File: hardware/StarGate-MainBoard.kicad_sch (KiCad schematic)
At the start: 168 parts, among them IC1 TB6612FNG, IC3 TB6612FNG, IC7 SGTL5000, J1 PJ-037A, J10 Conn_01x02_Pin, J11 Conn_01x03_Male, J12 Conn_01x02_Pin, J13 Conn_01x02_Pin, J14 Conn_01x02_Pin, J15 Conn_01x02_Pin, J16 Conn_01x02_Pin, J17 Conn_01x02_Pin, J18 Conn_01x02_Pin, J19 Conn_01x02_Pin, J2 Conn_01x03_Socket, J20 Conn_01x02_Pin, J21 Conn_01x02_Pin, J22 Conn_01x02_Pin, J23 Conn_01x02_Pin, J24 Conn_01x03_Socket, J26 Micro_SD_Card_Det, J27 Conn_01x03_Male, J28 Conn_01x02_Pin, J29 Conn_01x02_Pin, J3 Conn_01x02_Pin, J30 Conn_01x02_Pin, J31 Conn_01x02_Pin, J32 Conn_01x03_Male, J33 Conn_01x02_Pin, J34 USB_C_Receptacle, J4 Conn_01x04_Pin, J5 Conn_01x02_Pin, J6 Conn_01x02_Pin, J7 Conn_01x02_Pin, J8 Conn_01x02_Pin, J9 Conn_01x02_Pin, Q1 FDN340P, Q12 PMOS, Q2 FDN337N, Q3 N0400P-ZK-E1-AY, SW1 SW_Push_Dual, SW2 SW_Push_Dual, U1 SN74LVC1T45DBV, U10 AZ1084-1.8, U11 USBLC6-4SC6, U12 STMPS2151STR, U2 PCA9685, U32 FM6124, U6 ESP32-S3-WROOM-1-N16R2, U7 MC33063ADR, U8 TPA6017A2, U9 RT6219, X1 SG-210SDF (11.2896MHz)

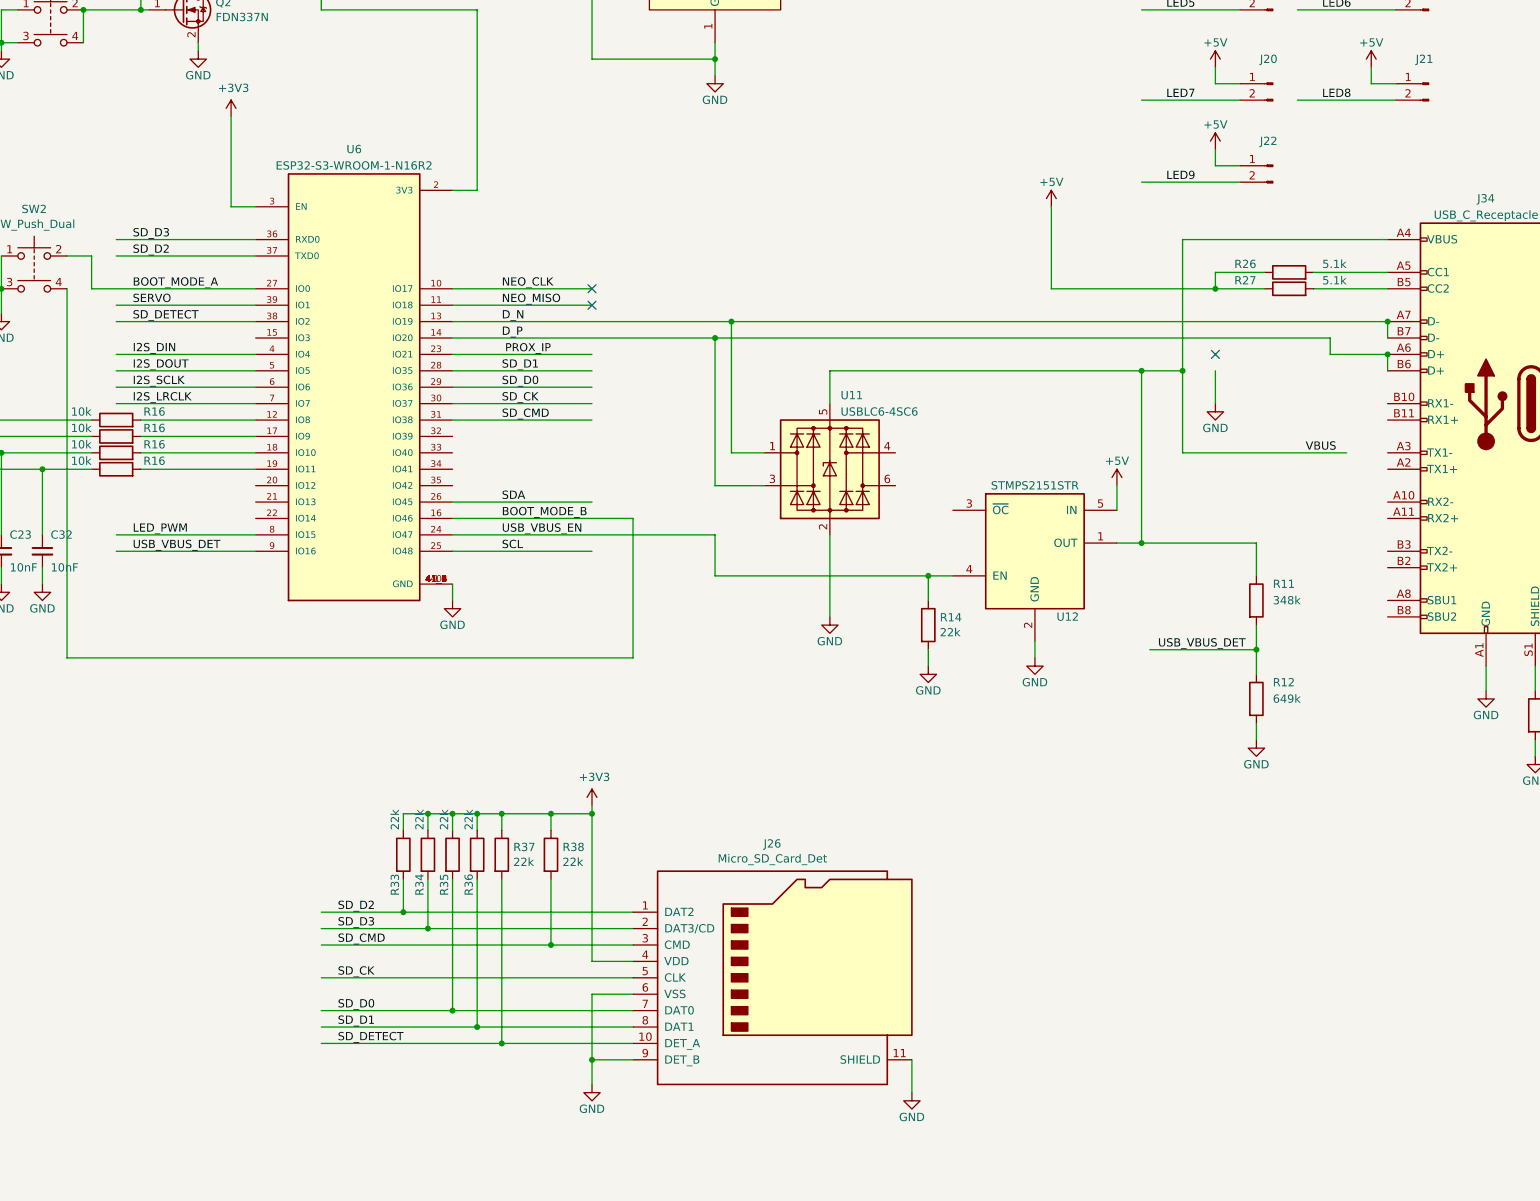
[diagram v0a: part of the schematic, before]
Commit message: Added JTAG Port
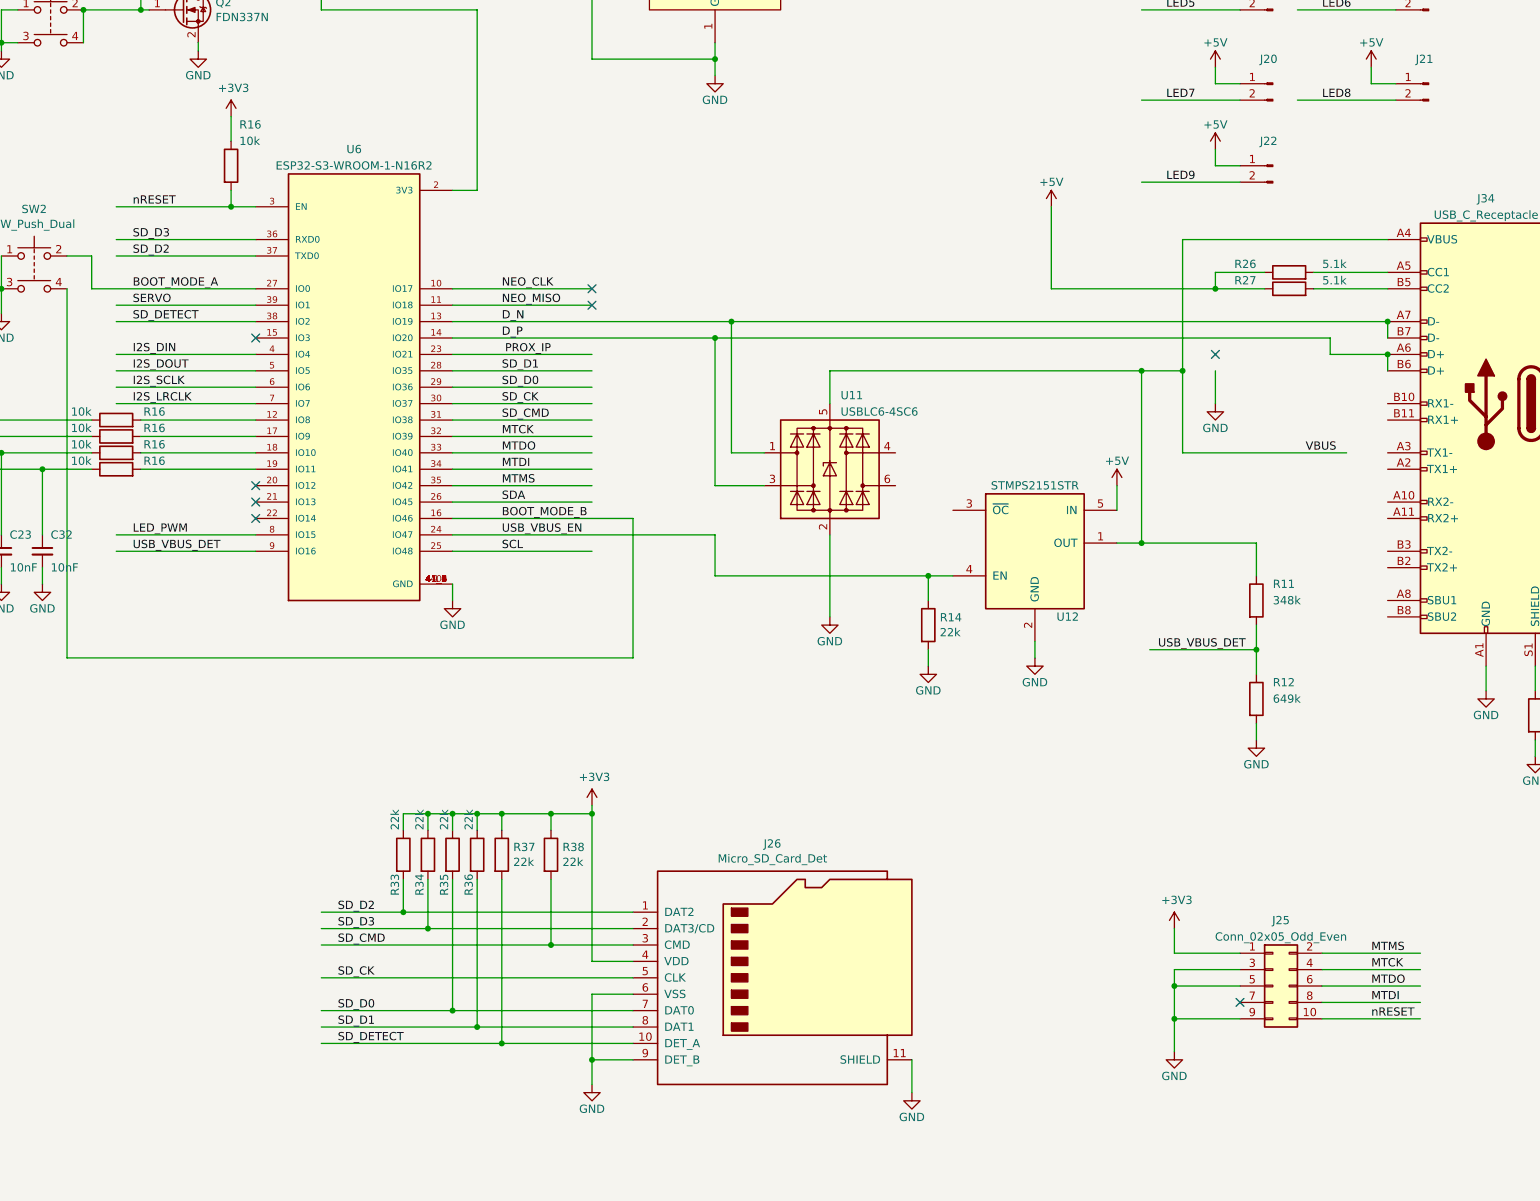
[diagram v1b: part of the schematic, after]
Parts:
- added J25: Conn_02x05_Odd_Even, Connector_PinHeader_2.54mm:PinHeader_2x05_P2.54mm_Vertical, symbol Connector_Generic:Conn_02x05_Odd_Even
- added R16: 10k, Resistor_SMD:R_0603_1608Metric, symbol Device:R
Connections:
- net +3V3: now also J25.1 (Pin_1), R16.1; no longer U6.3 (EN)
- net GND: now also J25.3 (Pin_3), J25.5 (Pin_5), J25.9 (Pin_9)
- net MTCK: now reaches U6.32 (IO39)
- net MTCK: now also J25.4 (Pin_4)
- net MTDO: now reaches U6.33 (IO40)
- net MTDO: now also J25.6 (Pin_6)
- net MTDI: now reaches U6.34 (IO41)
- net MTDI: now also J25.8 (Pin_8)
- net MTMS: now reaches U6.35 (IO42)
- net MTMS: now also J25.2 (Pin_2)
- new net nRESET: J25.10 (Pin_10), R16.2, U6.3 (EN)
- no-connect marks 38 -> 43

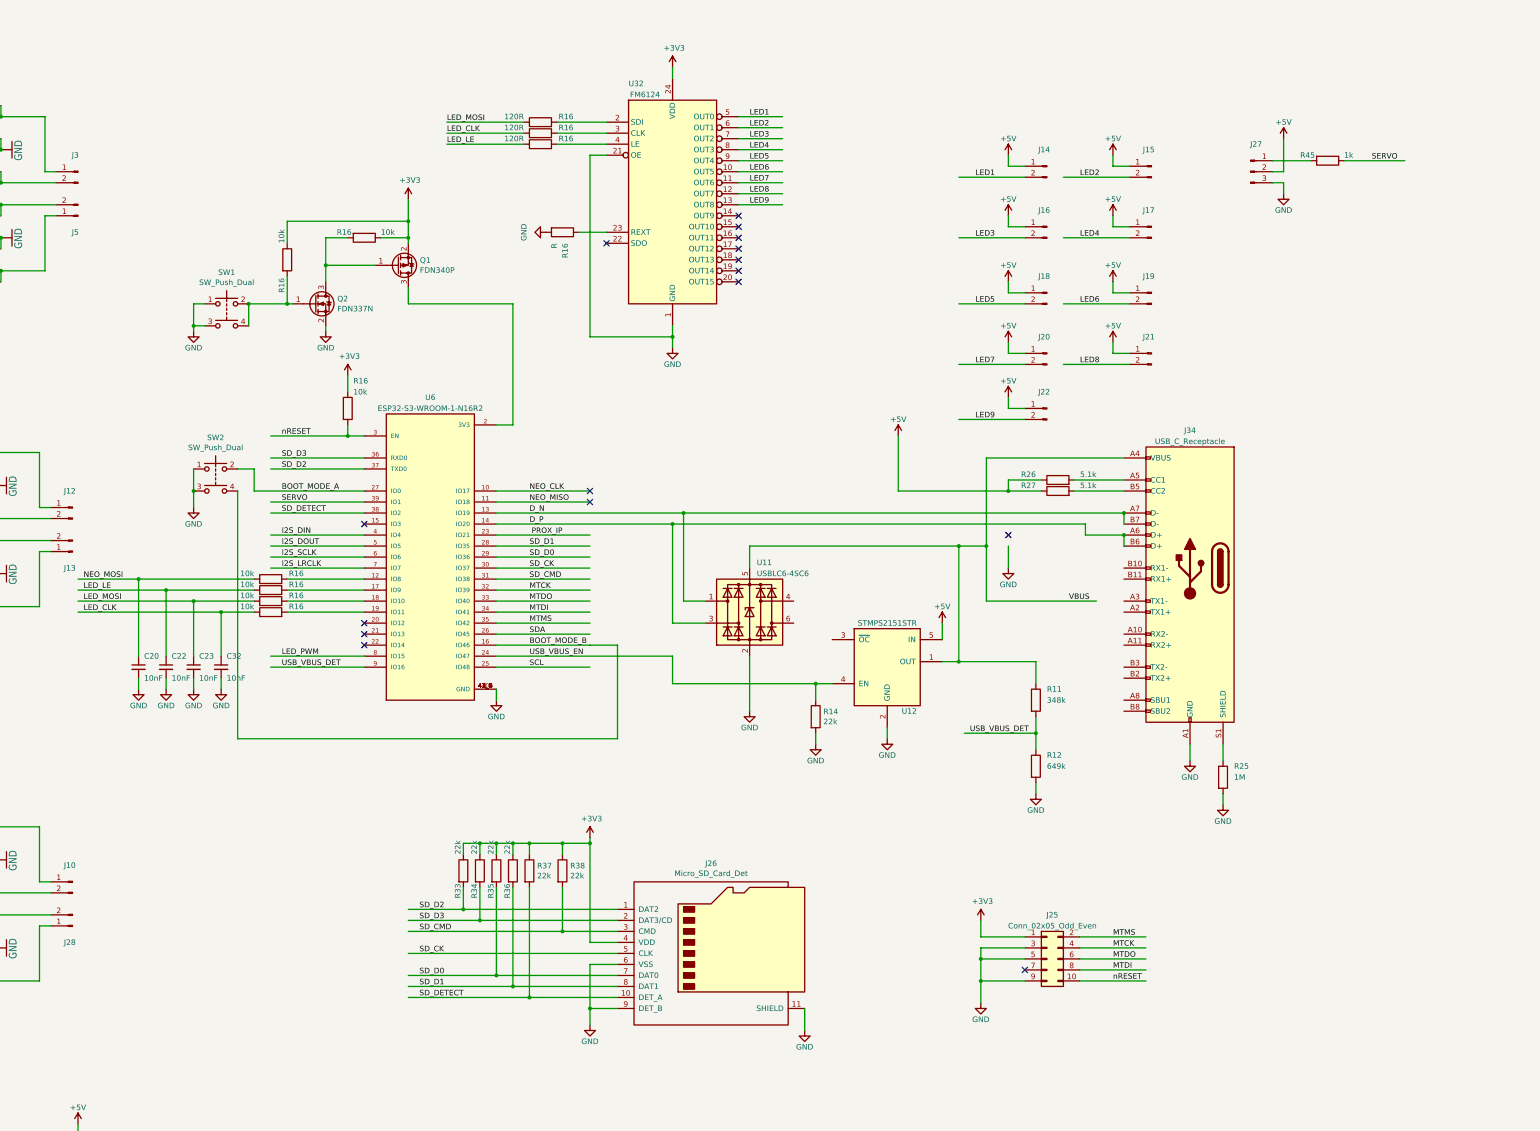
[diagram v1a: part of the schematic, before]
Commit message: Added CAP to reset line
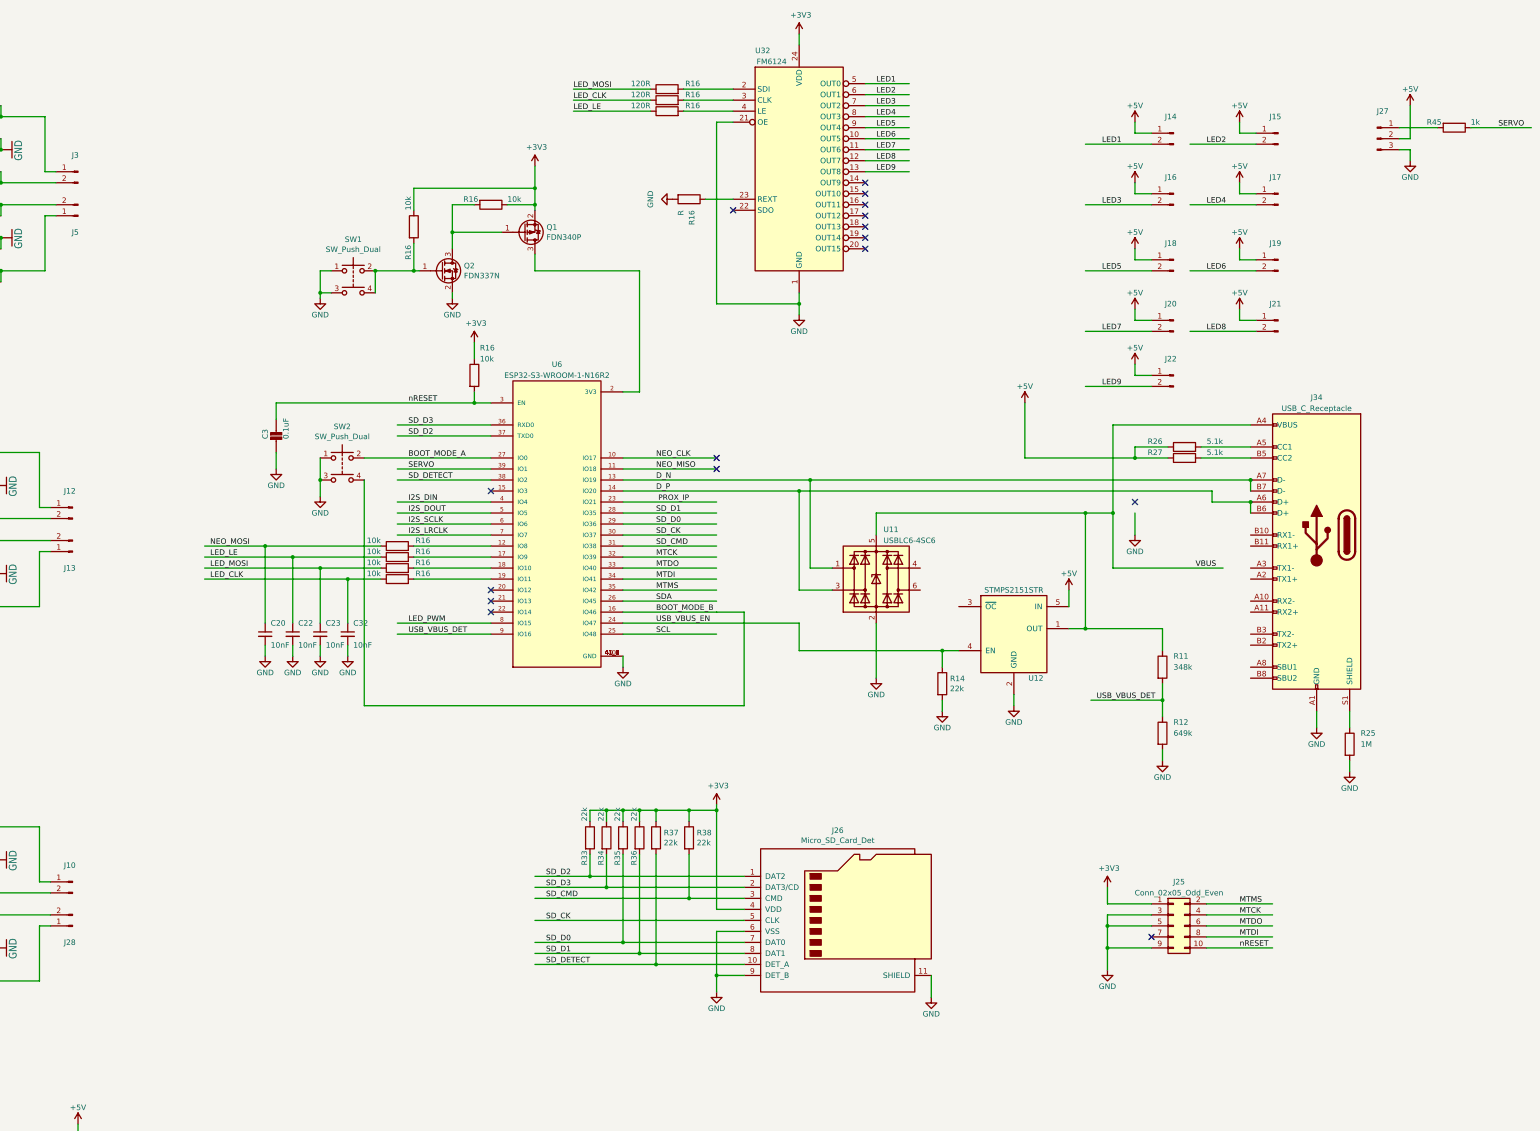
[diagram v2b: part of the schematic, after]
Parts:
- added C3: 0.1uF, Capacitor_SMD:C_0805_2012Metric, symbol Adafruit Motor HAT rev A-eagle-import:CAP_CERAMIC0805-NOOUTLINE
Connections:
- net GND: now also C3.2
- net nRESET: now also C3.1
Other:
- moved on the sheet: C20, C22, C23, C32, J14, J15, J16, J17, J18, J19, J20, J21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
